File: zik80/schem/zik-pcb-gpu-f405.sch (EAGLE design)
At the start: 14 parts

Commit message: Basic gpu pcb schem is done! Need to verify, and route, and good to go?
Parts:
- added C1, C4, C6, C7: .1uF, rcl:C-EU025-025X050
- added C3: ,1uF, rcl:C-EU025-025X050
- added C8, C9: 2.2uF, rcl:C-EU025-025X050
- added IOHDR, VGAHDR: (no value), pinhead:PINHD-1X6
- added LED1: (no value), SparkFun-LED:LED5MM
- added R1, R2, R3, R4, R5, R6, R7: (no value), rcl:R-US_0207/10
- added S1: SWITCH-MOMENTARY-2PTH, SparkFun-Electromechanical:SWITCH-MOMENTARY-2PTH
- added VIDEOHDR: (no value), pinhead:PINHD-1X8
- renumbered JP5 to ISPJTAG
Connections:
- removed net N$2: C2.1, GPUOSC.2, U$1.PH0/OSC_IN(5T)
- new net BOOT0: JP4.12, U$1.BOOT0
- new net N$10: VIDEOHDR.6
- new net N$3: LED1.A, R1.2
- new net N$5: R4.2, R5.2, VGAHDR.5
- new net N$8: R6.2, R7.2, VGAHDR.6
- new net NRST: JP1.7, S1.2, U$1.NRST
- new net PA0: JP1.14, U$1.PA0/ADC123_IN0(5T)
- new net PA1: JP1.15, U$1.PA1/ADC123_IN1(5T)
- new net PA10: JP3.11, U$1.PA10/TIM1_CH3/USART1_RX(5T), VIDEOHDR.3
- new net PA11: JP3.12, U$1.PA11/TIM1_CH4/CANRX/USBDM(5T)
- new net PA12: JP3.13, U$1.PA12/CANTX/USBDP(5T), VIDEOHDR.5
- new net PA2: JP1.16, U$1.PA2/ADC123_IN2(5T)
- new net PA3: JP2.1, U$1.PA3/ADC123_IN3(5T)
- new net PA4: JP2.4, U$1.PA4/ADC12_IN4
- new net PA5: JP2.5, U$1.PA5/ADC12_IN5
- new net PA6: JP2.6, U$1.PA6/ADC12_IN6(5T)
- new net PA7: JP2.7, U$1.PA7/TIM1_CH1N/ADC12_IN7(FT)
- new net PA8: JP3.9, U$1.PA8/TIM1_CH1(5T), VIDEOHDR.1
- new net PA9: JP3.10, U$1.PA9/TIM1_CH2/USART1_TX(5T), VIDEOHDR.2
- new net PB0: JP2.10, U$1.PB0/TIM1_CH2N/ADC12_IN8(5T)
- new net PB1: JP2.11, U$1.PB1/TIM1_CH3N/ADC12_IN9(5T)
- new net PB10: JP2.13, U$1.PB10/I2C2_SCL(5T), VGAHDR.1
- new net PB11: JP2.14, U$1.PB11/I2C2_SDA(5T), VGAHDR.2
- new net PB12: IOHDR.6, JP3.1, U$1.PB12(5T)
- new net PB13: JP3.2, U$1.PB13/SPI2_SCK(5T)
- new net PB14: JP3.3, U$1.PB14/SPI2_MISO(5T)
- new net PB15: JP3.4, U$1.PB15/SPI2_MOSI(5T)
- new net PB2: JP2.12, U$1.PB2/BOOT1(5T)
- new net PB5: JP4.9, U$1.PB5(5T)
- new net PB6: JP4.10, U$1.PB6/I2C1_SCL/USART1_TX/TIM4_CH1(5T), VIDEOHDR.7
- new net PB7: JP4.11, U$1.PB7/I2C1_SDA/USART1_RX/TIM4_CH2(5T), VIDEOHDR.8
- new net PB8: JP4.13, U$1.PB8/TIM10_CH1/TIM4_CH3(5T)
- new net PB9: JP4.14, U$1.PB9/TIM11_CH1/TIM4_CH4(5T)
- new net PC0: JP1.8, R3.1, U$1.PC0/ADC123_IN10(5T)
- new net PC1: JP1.9, R2.1, U$1.PC1/ADC123_IN11(5T)
- new net PC10: JP4.3, U$1.PC10(5T)
- new net PC11: JP4.4, U$1.PC11(5T)
- new net PC12: JP4.5, U$1.PC12(5T)
- new net PC13: JP1.2, U$1.PC13(5T)
- new net PC14: JP1.3, U$1.PC14/OSC32_IN(5T)
- new net PC15: JP1.4, U$1.PC15/OSC32_OUT(5T)
- new net PC2: JP1.10, R5.1, U$1.PC2/ADC123_IN12(5T)
- new net PC3: JP1.11, R4.1, U$1.PC3/ADC123_IN13(5T)
- new net PC4: JP2.8, R7.1, U$1.PC4/ADC12_IN14
- new net PC5: JP2.9, R6.1, U$1.PC5/ADC12_IN15
- new net PC6: IOHDR.1, JP3.5, U$1.PC6/TIM3_CH1/TIM_CH1/USART6_TX(5T)
- new net PC7: IOHDR.2, JP3.6, U$1.PC7/TIM3_CH2/TIM8_CH2/USART6_RX(5T)
- new net PC8: JP3.7, U$1.PC8/TIM3_CH3/TIM8_CH3(5T)
- new net PC9: JP3.8, U$1.PC9/TIM3_CH4/TIM8_CH4(5T)
- new net PD2: JP4.6, U$1.PD2/TIM3_ETR(5T)
- new net PH0: C2.1, GPUOSC.2, JP1.5, U$1.PH0/OSC_IN(5T)
- new net PH1: C5.1, GPUOSC.1, JP1.6, U$1.PH1/OSC_OUT(5T)
- new net VBAT: JP1.1, U$1.VBAT
- new net VCAP_1: C9.1, JP2.15, U$1.VCAP_1
- new net VCAP_2: C8.1, JP3.15, U$1.VCAP_2
- net +3V3: now also C1.1, C3.1, C4.1, C6.1, C7.1, JP1.13, JP2.16, JP2.3, JP3.16, JP4.16; no longer U$1.VBAT
- net +5V: now also R1.1
- net GND: now also C1.2, C3.2, C4.2, C6.2, C7.2, C8.2, C9.2, JP1.12, JP2.2, JP4.15, LED1.C, S1.1, VGAHDR.3
- net N$1: now also R2.2, R3.2; no longer C5.1, GPUOSC.1, U$1.PH1/OSC_OUT(5T)
- net PA13: now also JP3.14
- net PA14: now also JP4.1
- net PA15: now also JP4.2
- net PB3: now also JP4.7
- net PB4: now also JP4.8
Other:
- note added: "2.2uF = 22pF"
- note added: "Legend: + usart1 video + i2c p1: usart CK p2: TX p3: RX p4: CTS p5: RTS p6: p7: i2c scl p8: i2c sda"
- note added: "Legend: p1: Console TX (send from micro) p2: Console RX (receive to micro) p3: p4: p5: p6: vblank"
- note added: "Legend: p1: vsync: B10 p2: hsync: B11 p3: gnd p4: R p5: G p6: B"
- note added: "PC-low == RGB PB6/PB7 = i2c sda/scl ? conflict USART1? PB8 -> __? grab addr/data bus? PB9 -> __? heartbeat? PB10/11 == sync PB12 -> vblank __ = flags (hsync, vsync, heartbeat..) ?PC6-7 = console in/out .. use BoB jumpers PA8-PA12 = serial control in/out __ = address / data / control"
- note added: "Power LED 5V"
- note added: "Run to Vdd with .1uF decouple"
- note added: "TBD v2: - Add 2 brightness bits to VGA DAC - sync may need 80/100 resistor on some monitor - address/data/signal RAM bus"
- note added: "TBD: - check ISP again.. PCB: - drill holes in corner - version and website info - lavel +/-, and function points (hsync, vsync, etc)"
- note removed: "TBD: - VGA out with package .. drop screws, just solder points - serial in/out console standard header for project - serial in/out for cpu bus - i2c in/out for cpu bus - address/data/signal RAM bus - flag bus .. go high-Z, heartbeat, grab bus, etc - reset button on pcb? - check pins to breadboard - check ISP again.. - LED and resistor PCB: - drill holes in corner"
- moved on the sheet: PWRIN

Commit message: GPU schem is 'done'.. just need to read it over, verify against datasheet, etc; then off to routing!
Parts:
- added D1, D2, D3, D4, D5, D6: 1N5400, diode:1N5400
- added R10, R11, R12, R13, R14, R9: (no value), rcl:R-US_0207/10
- added R8: 10K, rcl:R-US_0207/10
- R1: value (none) -> 1K
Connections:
- removed net N$1: R2.2, R3.2
- new net N$12: D3.C, R11.1
- new net N$14: D4.C, R12.1
- new net N$17: D5.C, R13.1
- new net N$19: D6.C, R14.1
- new net N$4: D1.C, R9.1
- new net N$7: D2.C, R10.1
- new net N$9: R10.2, R2.2, R3.2, R9.2, VGAHDR.4
- net BOOT0: now also R8.2
- net GND: now also R8.1
- net N$5: now also R11.2, R12.2
- net N$8: now also R13.2, R14.2
- net PA2: now also IOHDR.1
- net PA3: now also IOHDR.2
- net PC6: now also D1.A, D3.A, D5.A; no longer IOHDR.1
- net PC7: now also D2.A, D4.A, D6.A; no longer IOHDR.2
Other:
- note added: "Brightness mix-in RRGGBBXX .. XX being brightness"
- note added: "Legend: p1: Console TX (send from micro): usart2 p2: Console RX (receive to micro): usart2 p3: p4: p5: p6: vblank"
- note added: "PA2-3 == serial console PA8-PA12 = serial control in/out PB6/PB7 = i2c sda/scl ? conflict USART1? PB8 -> __? grab addr/data bus? PB9 -> __? heartbeat? PB10/11 == sync PB12 -> vblank PC0-5 == RGB PC6-7 = brightness __ = flags (hsync, vsync, heartbeat..) __ = address / data / control"
- note added: "TBD v2: - sync may need 80/100 resistor on some monitor - address/data/signal RAM bus"
- note added: "TBD: PCB: - drill holes in corner - version and website info - label +/-, and function points (hsync, vsync, etc)"
- note removed: "Legend: p1: Console TX (send from micro) p2: Console RX (receive to micro) p3: p4: p5: p6: vblank"
- note removed: "PC-low == RGB PB6/PB7 = i2c sda/scl ? conflict USART1? PB8 -> __? grab addr/data bus? PB9 -> __? heartbeat? PB10/11 == sync PB12 -> vblank __ = flags (hsync, vsync, heartbeat..) ?PC6-7 = console in/out .. use BoB jumpers PA8-PA12 = serial control in/out __ = address / data / control"
- note removed: "TBD v2: - Add 2 brightness bits to VGA DAC - sync may need 80/100 resistor on some monitor - address/data/signal RAM bus"
- note removed: "TBD: - check ISP again.. PCB: - drill holes in corner - version and website info - lavel +/-, and function points (hsync, vsync, etc)"
- moved on the sheet: R2, R3, R4, R5, R6, R7, S1, VGAHDR

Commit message: few mods to the power pcb schem; finalizing the gpu pcb schem; started power pcb board layout.. woowoo!
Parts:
- added C10: .1uF, rcl:C-EU025-025X050
- added VBATPWRJP: (no value), pinhead:PINHD-1X2
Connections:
- net +3V3: now also C10.1, VBATPWRJP.2
- net GND: now also C10.2
- net PA11: now also VIDEOHDR.4
- net PA15: now also U$1.PA15/JTDI(5T)
- net VBAT: now also VBATPWRJP.1
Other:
- note added: "TBD v2: - sync may need 80/100 resistor on some monitor - address/data/signal RAM bus - add parallel caps to decoupling caps on stm32, so can have both a electrolytic + a tant on each, without sticking both through solder point? - extra GND plane via's!"
- note added: "TBD: PCB: - drill holes in corner - version and website info - label +/-, and function points (hsync, vsync, etc) - label pin1's, and pin count on headers - GND/GND pour"
- note removed: "Run to Vdd with .1uF decouple"
- note removed: "TBD v2: - sync may need 80/100 resistor on some monitor - address/data/signal RAM bus"
- note removed: "TBD: PCB: - drill holes in corner - version and website info - label +/-, and function points (hsync, vsync, etc)"
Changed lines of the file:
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@@
 <part name="D6" library="diode" deviceset="1N5400" device=""/>
 <part name="R14" library="rcl" deviceset="R-US_" device="0207/10"/>
+<part name="VBATPWRJP" library="pinhead" deviceset="PINHD-1X2" device=""/>
+<part name="C10" library="rcl" deviceset="C-EU" device="025-025X050" value=".1uF"/>
+<part name="GND14" library="supply1" deviceset="GND" device=""/>
 </parts>
 <sheets>
@@
 - drill holes in corner
 - version and website info
-- label +/-, and function points (hsync, vsync, etc)</text>
+- label +/-, and function points (hsync, vsync, etc)
+- label pin1's, and pin count on headers
+- GND/GND pour</text>
 <text x="74.93" y="130.81" size="2.54" layer="94">Break-out Headers</text>
 <text x="2.54" y="130.81" size="2.54" layer="94">ISP</text>
@@
 - GND</text>
 <text x="-30.48" y="25.4" size="1.778" layer="94" rot="R90">2.2uF = 22pF</text>
-<text x="44.45" y="62.23" size="1.778" layer="94">Run to Vdd with .1uF decouple</text>
-<text x="-181.61" y="50.8" size="3.81" layer="94">TBD v2:
+<text x="-191.77" y="27.94" size="3.81" layer="94">TBD v2:
 - sync may need 80/100 resistor on some monitor
-- address/data/signal RAM bus</text>
+- address/data/signal RAM bus
+- add parallel caps to decoupling caps on stm32, so
+can have both a electrolytic + a tant on each,
+without sticking both through solder point?
+- extra GND plane via's!</text>
 <text x="-54.61" y="-11.43" size="1.778" layer="94">Power LED 5V</text>
 <text x="266.7" y="107.95" size="2.54" layer="91">Legend:
@@
 p5: G
 p6: B</text>
-<text x="-181.61" y="-11.43" size="2.54" layer="91">PA2-3 == serial console
+<text x="-184.15" y="-40.64" size="2.54" layer="91">PA2-3 == serial console
 PA8-PA12 = serial control in/out
 PB6/PB7 = i2c sda/scl ? conflict USART1?
@@
 <instance part="D6" gate="1" x="204.47" y="39.37"/>
 <instance part="R14" gate="G$1" x="220.98" y="39.37"/>
+<instance part="VBATPWRJP" gate="G$1" x="-41.91" y="58.42" rot="R270"/>
+<instance part="C10" gate="G$1" x="-52.07" y="48.26"/>
+<instance part="GND14" gate="1" x="-52.07" y="36.83"/>
 </instances>
 <busses>
@@
 <label x="148.59" y="83.82" size="1.27" layer="95" rot="R180" xref="yes"/>
 </segment>
+<segment>
+<pinref part="VBATPWRJP" gate="G$1" pin="2"/>
+<wire x1="-41.91" y1="60.96" x2="-41.91" y2="71.12" width="0.1524" layer="91"/>
+<wire x1="-41.91" y1="71.12" x2="-52.07" y2="71.12" width="0.1524" layer="91"/>
+<label x="-54.61" y="71.12" size="1.27" layer="95" rot="R180" xref="yes"/>
+<pinref part="C10" gate="G$1" pin="1"/>
+<wire x1="-52.07" y1="71.12" x2="-54.61" y2="71.12" width="0.1524" layer="91"/>
+<wire x1="-52.07" y1="50.8" x2="-52.07" y2="71.12" width="0.1524" layer="91"/>
+<junction x="-52.07" y="71.12"/>
+</segment>
 </net>
 <net name="GND" class="0">
@@
 <wire x1="53.34" y1="-5.08" x2="53.34" y2="-7.62" width="0.1524" layer="91"/>
 </segment>
+<segment>
+<pinref part="C10" gate="G$1" pin="2"/>
+<wire x1="-52.07" y1="43.18" x2="-52.07" y2="39.37" width="0.1524" layer="91"/>
+<pinref part="GND14" gate="1" pin="GND"/>
+</segment>
 </net>
 <net name="PA15" class="0">
 <segment>
-<wire x1="74.93" y1="-33.02" x2="67.31" y2="-33.02" width="0.1524" layer="91"/>
+<wire x1="73.66" y1="-33.02" x2="67.31" y2="-33.02" width="0.1524" layer="91"/>
 <label x="67.31" y="-33.02" size="1.27" layer="95" rot="R180" xref="yes"/>
+<pinref part="U$1" gate="G$1" pin="PA15/JTDI(5T)"/>
 </segment>
 <segment>
@@
 </segment>
 <segment>
-<wire x1="207.01" y1="-27.94" x2="198.12" y2="-27.94" width="0.1524" layer="91"/>
+<wire x1="205.74" y1="-27.94" x2="198.12" y2="-27.94" width="0.1524" layer="91"/>
 <label x="198.12" y="-27.94" size="1.27" layer="95" rot="R180" xref="yes"/>
+<pinref part="VIDEOHDR" gate="A" pin="4"/>
 </segment>
 </net>
@@
 <segment>
 <pinref part="VIDEOHDR" gate="A" pin="7"/>
-<wire x1="205.74" y1="-35.56" x2="199.39" y2="-35.56" width="0.1524" layer="91"/>
-<wire x1="198.12" y1="-35.56" x2="199.39" y2="-35.56" width="0.1524" layer="91"/>
+<wire x1="205.74" y1="-35.56" x2="198.12" y2="-35.56" width="0.1524" layer="91"/>
 <label x="198.12" y="-35.56" size="1.27" layer="95" rot="R180" xref="yes"/>
 </segment>
@@
 <segment>
 <pinref part="U$1" gate="G$1" pin="VBAT"/>
-<wire x1="73.66" y1="58.42" x2="67.31" y2="58.42" width="0.1524" layer="91"/>
+<wire x1="73.66" y1="58.42" x2="69.85" y2="58.42" width="0.1524" layer="91"/>
 <label x="67.31" y="58.42" size="1.27" layer="95" rot="R180" xref="yes"/>
+<wire x1="69.85" y1="58.42" x2="67.31" y2="58.42" width="0.1524" layer="91"/>
+<wire x1="69.85" y1="58.42" x2="69.85" y2="71.12" width="0.1524" layer="91"/>
+<pinref part="VBATPWRJP" gate="G$1" pin="1"/>
+<wire x1="69.85" y1="71.12" x2="-39.37" y2="71.12" width="0.1524" layer="91"/>
+<wire x1="-39.37" y1="71.12" x2="-39.37" y2="60.96" width="0.1524" layer="91"/>
+<junction x="69.85" y="58.42"/>
 </segment>
 <segment>
@@
 </sheet>
 </sheets>
+<errors>
+</errors>
 </schematic>
 </drawing>

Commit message: rev1 of both power and gpu boards finalized, and elecrow gerber files generated!
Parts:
- renumbered VIDEOHDR to GPUHDR
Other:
- note removed: "TBD: PCB: - drill holes in corner - version and website info - label +/-, and function points (hsync, vsync, etc) - label pin1's, and pin count on headers - GND/GND pour"
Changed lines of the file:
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@@
 <setting verticaltext="up"/>
 </settings>
-<grid distance="0.05" unitdist="inch" unit="inch" style="dots" multiple="1" display="yes" altdistance="0.01" altunitdist="inch" altunit="inch"/>
+<grid distance="0.1" unitdist="inch" unit="inch" style="lines" multiple="1" display="no" altdistance="0.01" altunitdist="inch" altunit="inch"/>
 <layers>
 <layer number="1" name="Top" color="4" fill="1" visible="no" active="no"/>
@@
 <part name="R7" library="rcl" deviceset="R-US_" device="0207/10"/>
 <part name="IOHDR" library="pinhead" deviceset="PINHD-1X6" device=""/>
-<part name="VIDEOHDR" library="pinhead" deviceset="PINHD-1X8" device=""/>
+<part name="GPUHDR" library="pinhead" deviceset="PINHD-1X8" device=""/>
 <part name="R8" library="rcl" deviceset="R-US_" device="0207/10" value="10K"/>
 <part name="GND13" library="supply1" deviceset="GND" device=""/>
@@
 - 3.3
 - GND</text>
-<text x="-181.61" y="73.66" size="3.81" layer="94">TBD:
-PCB:
-- drill holes in corner
-- version and website info
-- label +/-, and function points (hsync, vsync, etc)
-- label pin1's, and pin count on headers
-- GND/GND pour</text>
 <text x="74.93" y="130.81" size="2.54" layer="94">Break-out Headers</text>
 <text x="2.54" y="130.81" size="2.54" layer="94">ISP</text>
@@
 - GND</text>
 <text x="-30.48" y="25.4" size="1.778" layer="94" rot="R90">2.2uF = 22pF</text>
-<text x="-191.77" y="27.94" size="3.81" layer="94">TBD v2:
+<text x="-168.91" y="86.36" size="3.81" layer="94">TBD v2:
 - sync may need 80/100 resistor on some monitor
 - address/data/signal RAM bus
@@
 <instance part="R7" gate="G$1" x="219.71" y="91.44"/>
 <instance part="IOHDR" gate="A" x="207.01" y="1.27"/>
-<instance part="VIDEOHDR" gate="A" x="208.28" y="-30.48"/>
+<instance part="GPUHDR" gate="A" x="208.28" y="-30.48"/>
 <instance part="R8" gate="G$1" x="53.34" y="0" rot="R90"/>
 <instance part="GND13" gate="1" x="53.34" y="-10.16"/>
@@
 </segment>
 <segment>
-<pinref part="VIDEOHDR" gate="A" pin="1"/>
+<pinref part="GPUHDR" gate="A" pin="1"/>
 <wire x1="205.74" y1="-20.32" x2="198.12" y2="-20.32" width="0.1524" layer="91"/>
 <label x="198.12" y="-20.32" size="1.27" layer="95" rot="R180" xref="yes"/>
@@
 </segment>
 <segment>
-<pinref part="VIDEOHDR" gate="A" pin="2"/>
+<pinref part="GPUHDR" gate="A" pin="2"/>
 <wire x1="205.74" y1="-22.86" x2="198.12" y2="-22.86" width="0.1524" layer="91"/>
 <label x="198.12" y="-22.86" size="1.27" layer="95" rot="R180" xref="yes"/>
@@
 </segment>
 <segment>
-<pinref part="VIDEOHDR" gate="A" pin="3"/>
+<pinref part="GPUHDR" gate="A" pin="3"/>
 <wire x1="205.74" y1="-25.4" x2="198.12" y2="-25.4" width="0.1524" layer="91"/>
 <label x="198.12" y="-25.4" size="1.27" layer="95" rot="R180" xref="yes"/>
@@
 <wire x1="205.74" y1="-27.94" x2="198.12" y2="-27.94" width="0.1524" layer="91"/>
 <label x="198.12" y="-27.94" size="1.27" layer="95" rot="R180" xref="yes"/>
-<pinref part="VIDEOHDR" gate="A" pin="4"/>
+<pinref part="GPUHDR" gate="A" pin="4"/>
 </segment>
 </net>
@@
 </segment>
 <segment>
-<pinref part="VIDEOHDR" gate="A" pin="5"/>
+<pinref part="GPUHDR" gate="A" pin="5"/>
 <wire x1="205.74" y1="-30.48" x2="198.12" y2="-30.48" width="0.1524" layer="91"/>
 <label x="198.12" y="-30.48" size="1.27" layer="95" rot="R180" xref="yes"/>
@@
 </segment>
 <segment>
-<pinref part="VIDEOHDR" gate="A" pin="7"/>
+<pinref part="GPUHDR" gate="A" pin="7"/>
 <wire x1="205.74" y1="-35.56" x2="198.12" y2="-35.56" width="0.1524" layer="91"/>
 <label x="198.12" y="-35.56" size="1.27" layer="95" rot="R180" xref="yes"/>
@@
 </segment>
 <segment>
-<pinref part="VIDEOHDR" gate="A" pin="8"/>
+<pinref part="GPUHDR" gate="A" pin="8"/>
 <wire x1="205.74" y1="-38.1" x2="198.12" y2="-38.1" width="0.1524" layer="91"/>
 <label x="198.12" y="-38.1" size="1.27" layer="95" rot="R180" xref="yes"/>
@@
 <net name="N$10" class="0">
 <segment>
-<pinref part="VIDEOHDR" gate="A" pin="6"/>
+<pinref part="GPUHDR" gate="A" pin="6"/>
 <wire x1="205.74" y1="-33.02" x2="198.12" y2="-33.02" width="0.1524" layer="91"/>
 </segment>

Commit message: Made a couple notes on power and gpu schems, of things needing correction; fiddled with vga out on real pcb.. works!
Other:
- note added: "BUG in r1: JTAG reset is not working; have to hit manual reset so flashing and post-flash can work right - change jtag reset from 56 JNTRST to real master reset pin 7.. all good then"
- note added: "Resistors are alternating 1K and 2K values"
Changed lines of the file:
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@@
 <text x="180.34" y="81.28" size="1.778" layer="91">Brightness mix-in
 RRGGBBXX .. XX being brightness</text>
+<text x="254" y="80.01" size="2.54" layer="91">Resistors are
+alternating 1K and 2K
+values</text>
+<text x="-186.69" y="27.94" size="5.08" layer="94">BUG in r1:
+JTAG reset is not working;
+have to hit manual reset
+so flashing and post-flash
+can work right
+- change jtag reset from 56 JNTRST
+to real master reset pin 7.. all good then</text>
 </plain>
 <instances>

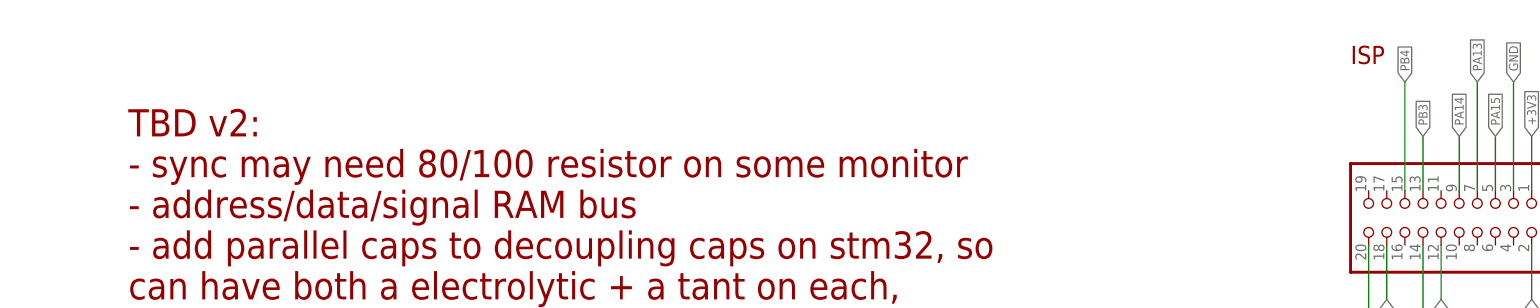
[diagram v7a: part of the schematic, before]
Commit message: Added note to gpu schem
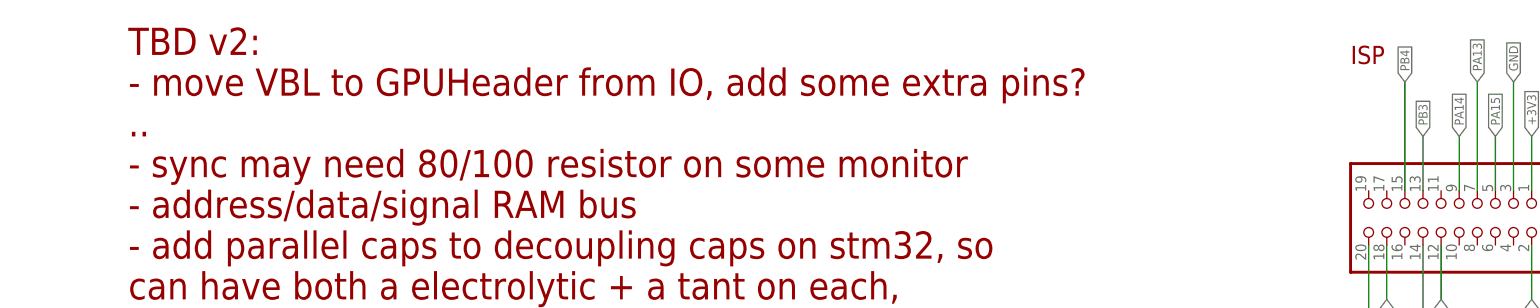
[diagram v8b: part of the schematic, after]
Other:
- note added: "TBD v2: - move VBL to GPUHeader from IO, add some extra pins? .. - sync may need 80/100 resistor on some monitor - address/data/signal RAM bus - add parallel caps to decoupling caps on stm32, so can have both a electrolytic + a tant on each, without sticking both through solder point? - extra GND plane via's!"
- note removed: "TBD v2: - sync may need 80/100 resistor on some monitor - address/data/signal RAM bus - add parallel caps to decoupling caps on stm32, so can have both a electrolytic + a tant on each, without sticking both through solder point? - extra GND plane via's!"
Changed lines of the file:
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@@
 <text x="-30.48" y="25.4" size="1.778" layer="94" rot="R90">2.2uF = 22pF</text>
 <text x="-168.91" y="86.36" size="3.81" layer="94">TBD v2:
+- move VBL to GPUHeader from IO, add some extra pins?
+..
 - sync may need 80/100 resistor on some monitor
 - address/data/signal RAM bus
